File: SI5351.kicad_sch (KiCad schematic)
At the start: 15 parts, among them U8 Si5351A, Y3 25MHz

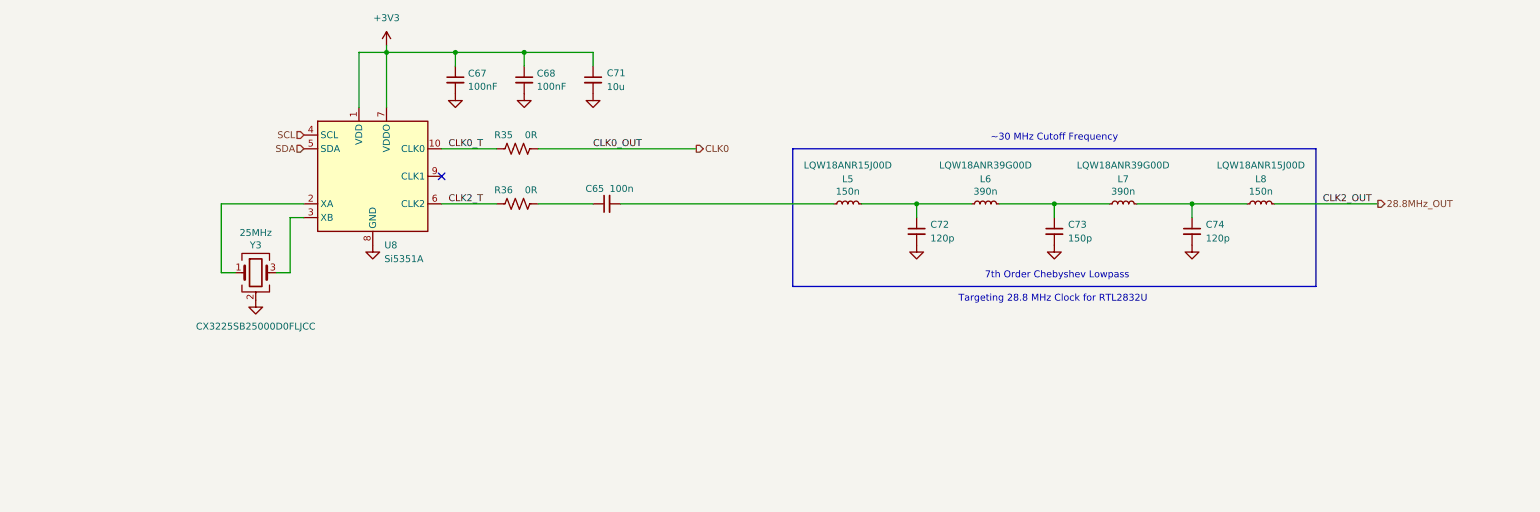
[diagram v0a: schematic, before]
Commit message: Schematic progress
I keep forgetting that I'm just making a panadapter here and not a full blown SDR...oops
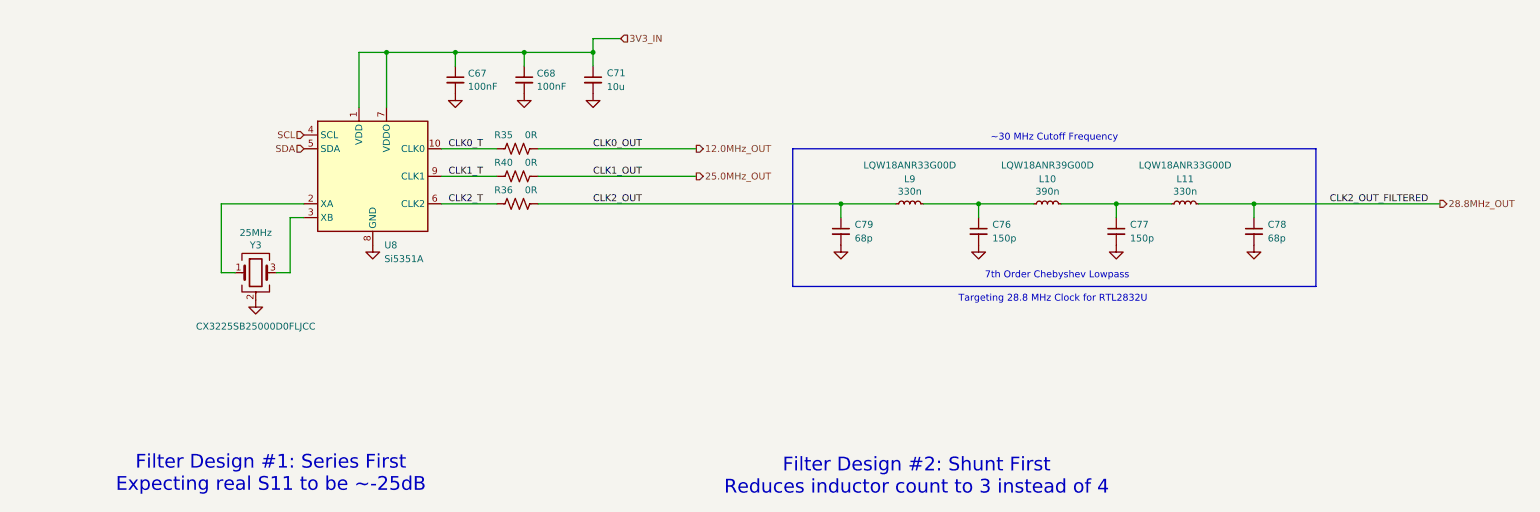
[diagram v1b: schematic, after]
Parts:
- removed C65: 100n, libraries:Worthington_C_0402, symbol Device:C_Small
- removed C72, C74: 120p, Capacitor_SMD:C_0603_1608Metric_Pad1.08x0.95mm_HandSolder, symbol Device:C_Small
- removed C73: 150p, Capacitor_SMD:C_0603_1608Metric_Pad1.08x0.95mm_HandSolder, symbol Device:C_Small
- removed L5, L8: 150n, Inductor_SMD:L_0603_1608Metric, symbol Device:L_Small
- removed L6, L7: 390n, symbol Device:L_Small
- added C76, C77: 150p, Capacitor_SMD:C_0603_1608Metric_Pad1.08x0.95mm_HandSolder, symbol Device:C_Small
- added C78, C79: 68p, Capacitor_SMD:C_0603_1608Metric_Pad1.08x0.95mm_HandSolder, symbol Device:C_Small
- added L10: 390n, libraries:Worthington_L_0603, symbol Device:L_Small
- added L11, L9: 330n, libraries:Worthington_L_0603, symbol Device:L_Small
- added R40: 0R, Resistor_SMD:R_0603_1608Metric_Pad0.98x0.95mm_HandSolder, symbol Device:R_US
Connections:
- net 28.8MHz_OUT: now also C78.1, L11.1
- net GND: now also C76.2, C77.2, C78.2, C79.2
- net CLK1_T: now reaches U8.9 (CLK1)
- net CLK1_T: now also R40.1
- net CLK2_OUT: now reaches R36.2
- net CLK2_OUT: now also C79.1, L9.2
- net +3V3 renamed 3V3_IN
- net CLK0 renamed 12.0MHz_OUT
- new net: C77.1, L10.1, L11.2
- new net: C76.1, L10.2, L9.1
- new net 25.0MHz_OUT: R40.2
- no-connect marks 1 -> 0
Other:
- note added: "Filter Design #1: Series First Expecting real S11 to be ~-25dB"
- note added: "Filter Design #2: Shunt First Reduces inductor count to 3 instead of 4"

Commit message: Schematic progress
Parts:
- removed L10: 390n, libraries:Worthington_L_0603, symbol Device:L_Small
- removed L11, L9: 330n, libraries:Worthington_L_0603, symbol Device:L_Small
- added L18, L20: 330n, libraries:Worthington_L_0603, symbol Device:L_Small
- added L19: 390n, libraries:Worthington_L_0603, symbol Device:L_Small
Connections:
- net 28.8MHz_OUT: now also L20.2
- net CLK2_OUT: now also L18.1
- net at C77.1: now also L19.2, L20.1
- net at C76.1: now also L18.2, L19.1

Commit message: Schematic progress
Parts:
- removed C78: 68p, Capacitor_SMD:C_0603_1608Metric_Pad1.08x0.95mm_HandSolder, symbol Device:C_Small
- added C123, C81: 100n, libraries:Worthington_C_0201, symbol Device:C_Small
- added C92: 68p, libraries:Worthington_C_0201, symbol Device:C_Small
- added R77: 0R, libraries:Worthington_R_0201, symbol Device:R_US
- added R78, R79: 4k7, libraries:Worthington_R_0201, symbol Device:R_Small_US
- C67, C68: value 100nF -> 100n; footprint Capacitor_SMD:C_0603_1608Metric_Pad1.08x0.95mm_HandSolder -> libraries:Worthington_C_0201; DigiKey (none) -> 445-15903-1-ND; Manufacturer Part Number (none) -> C0603X6S1C104K030BC; Voltage (none) -> 16V
- C71: footprint libraries:Worthington_C_0603 -> libraries:Worthington_C_0402; DigiKey (none) -> 4713-GMC04X5R106M10NTCT-ND; Manufacturer Part Number (none) -> GMC04X5R106M10NT; Voltage (none) -> 10V
- C76, C77: footprint Capacitor_SMD:C_0603_1608Metric_Pad1.08x0.95mm_HandSolder -> libraries:Worthington_C_0201; DigiKey (none) -> 4713-GMC02CG151F50NTCT-ND; Manufacturer Part Number (none) -> GMC02CG151F50NT; Voltage (none) -> 50V
- C79: footprint Capacitor_SMD:C_0603_1608Metric_Pad1.08x0.95mm_HandSolder -> libraries:Worthington_C_0201; DigiKey (none) -> 4713-GMC02CG680F50NTCT-ND; Manufacturer Part Number (none) -> GMC02CG680F50NT; Voltage (none) -> 50V
- R35, R36, R40: footprint Resistor_SMD:R_0603_1608Metric_Pad0.98x0.95mm_HandSolder -> libraries:Worthington_R_0201
- U8: value Si5351A -> SI5351B-B-GM1; footprint Package_SO:MSOP-10_3x3mm_P0.5mm -> Package_DFN_QFN:QFN-16-1EP_3x3mm_P0.5mm_EP1.45x1.45mm
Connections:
- net 25.0MHz_OUT: now also R36.2; no longer R40.2
- net 28.8MHz_OUT: now also C92.1
- net 3V3_IN: now also U8.11 (VDDOD), U8.14 (VDDOC), U8.16 (VDD), U8.8 (VDDOB), U8.9 (VDDOA), C123.1, C81.1, R78.2, R79.2; no longer U8.1 (VDD), U8.7 (VDDO)
- net CLK1_T: now also R36.1, U8.7 (CLK1); no longer R40.1, U8.9 (CLK1)
- net CLK2_T: now also R40.1, U8.13 (CLK2); no longer R36.1, U8.6 (CLK2)
- net GND: now also U8.15 (GND), U8.EP (GND), C123.2, C81.2, C92.2; no longer U8.8 (GND)
- net SCL: now also R78.1
- net SDA: now also R79.1
- net at Y3.1: now also U8.1 (XA); no longer U8.2 (XA)
- net at Y3.3: now also U8.2 (XB); no longer U8.3 (XB)
- net CLK2_OUT renamed CLK2
- net CLK2: now also R40.2; no longer R36.2
- new net CLK3_50R_T: R77.1, U8.12 (CLK3)
- new net EXT_CLK_OUT: R77.2
- new net VCXO_IN: U8.3 (VC)
- new net ~{CLK_OUT_EN}: U8.6 (OEB)
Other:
- moved on the sheet: R35, Y3

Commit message: Schematic and PCB progress
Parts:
- renumbered C81 to C66, C123 to C67, C67 to C68, C68 to C69, C71 to C70, C79 to C71, C76 to C72, C77 to C73, C92 to C74, L18 to L5, L19 to L6, L20 to L7, R79 to R50, R78 to R51, R35 to R52, R36 to R53, R40 to R54, R77 to R55, U8 to U10, Y3 to Y1
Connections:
- net GND: now also U10.17 (GND); no longer U10.EP (GND)
- net at Y1.1: now also U10.2 (XB); no longer U10.1 (XA)
- net at Y1.3: now also U10.1 (XA); no longer U10.2 (XB)
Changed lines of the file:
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@@
 		(in_pos_files yes)
 		(dnp no)
-		(property "Reference" "C71"
+		(property "Reference" "C70"
 			(at 171.45 99.0662 0)
 			(show_name no)
@@
 			(project "PiZero_RTL_Panadapter"
 				(path "/9dbbaad8-804a-4efe-a989-bc17c5acbd91/6fef9fcc-556a-4b57-952e-8adf007c871b"
-					(reference "C71")
+					(reference "C70")
 					(unit 1)
 				)
@@
 		(in_pos_files yes)
 		(dnp no)
-		(property "Reference" "L20"
+		(property "Reference" "L7"
 			(at 269.24 118.618 90)
 			(show_name no)
@@
 			(project "PiZero_RTL_Panadapter"
 				(path "/9dbbaad8-804a-4efe-a989-bc17c5acbd91/6fef9fcc-556a-4b57-952e-8adf007c871b"
-					(reference "L20")
+					(reference "L7")
 					(unit 1)
 				)
@@
 		(lib_id "Device:Crystal_GND24")
 		(at 78.74 138.43 0)
-		(unit 1)
-		(body_style 1)
-		(exclude_from_sim no)
-		(in_bom yes)
-		(on_board yes)
-		(in_pos_files yes)
-		(dnp no)
-		(property "Reference" "Y3"
+		(mirror y)
+		(unit 1)
+		(body_style 1)
+		(exclude_from_sim no)
+		(in_bom yes)
+		(on_board yes)
+		(in_pos_files yes)
+		(dnp no)
+		(property "Reference" "Y1"
 			(at 78.74 133.35 0)
 			(show_name no)
@@
 			(project "PiZero_RTL_Panadapter"
 				(path "/9dbbaad8-804a-4efe-a989-bc17c5acbd91/6fef9fcc-556a-4b57-952e-8adf007c871b"
-					(reference "Y3")
+					(reference "Y1")
 					(unit 1)
 				)
@@
 		(in_pos_files yes)
 		(dnp no)
-		(property "Reference" "L19"
+		(property "Reference" "L6"
 			(at 243.84 118.618 90)
 			(show_name no)
@@
 			(project "PiZero_RTL_Panadapter"
 				(path "/9dbbaad8-804a-4efe-a989-bc17c5acbd91/6fef9fcc-556a-4b57-952e-8adf007c871b"
-					(reference "L19")
+					(reference "L6")
 					(unit 1)
 				)
@@
 		(in_pos_files yes)
 		(dnp no)
-		(property "Reference" "C81"
+		(property "Reference" "C66"
 			(at 130.81 99.0662 0)
 			(show_name no)
@@
 			(project "PiZero_RTL_Panadapter"
 				(path "/9dbbaad8-804a-4efe-a989-bc17c5acbd91/6fef9fcc-556a-4b57-952e-8adf007c871b"
-					(reference "C81")
+					(reference "C66")
 					(unit 1)
 				)
@@
 		(in_pos_files yes)
 		(dnp no)
-		(property "Reference" "C68"
+		(property "Reference" "C69"
 			(at 161.29 99.0662 0)
 			(show_name no)
@@
 			(project "PiZero_RTL_Panadapter"
 				(path "/9dbbaad8-804a-4efe-a989-bc17c5acbd91/6fef9fcc-556a-4b57-952e-8adf007c871b"
-					(reference "C68")
+					(reference "C69")
 					(unit 1)
 				)
@@
 		(in_pos_files yes)
 		(dnp no)
-		(property "Reference" "U8"
+		(property "Reference" "U10"
 			(at 108.458 119.888 0)
 			(show_name no)
@@
 		(pin "13"
 		)
-		(pin "EP"
+		(pin "17"
 		)
 		(pin "16"
@@
 			(project "PiZero_RTL_Panadapter"
 				(path "/9dbbaad8-804a-4efe-a989-bc17c5acbd91/6fef9fcc-556a-4b57-952e-8adf007c871b"
-					(reference "U8")
+					(reference "U10")
 					(unit 1)
 				)
@@
 		(in_pos_files yes)
 		(dnp no)
-		(property "Reference" "C79"
+		(property "Reference" "C71"
 			(at 208.28 127.0062 0)
 			(show_name no)
@@
 			(project "PiZero_RTL_Panadapter"
 				(path "/9dbbaad8-804a-4efe-a989-bc17c5acbd91/6fef9fcc-556a-4b57-952e-8adf007c871b"
-					(reference "C79")
+					(reference "C71")
 					(unit 1)
 				)
@@
 		(dnp no)
 		(fields_autoplaced yes)
-		(property "Reference" "#PWR0132"
+		(property "Reference" "#PWR0102"
 			(at 138.43 109.22 0)
 			(hide yes)
@@
 			(project "PiZero_RTL_Panadapter"
 				(path "/9dbbaad8-804a-4efe-a989-bc17c5acbd91/6fef9fcc-556a-4b57-952e-8adf007c871b"
-					(reference "#PWR0132")
+					(reference "#PWR0102")
 					(unit 1)
 				)
@@
 		(in_pos_files yes)
 		(dnp no)
-		(property "Reference" "R79"
+		(property "Reference" "R50"
 			(at 69.342 105.156 0)
 			(show_name no)
@@
 			(project "PiZero_RTL_Panadapter"
 				(path "/9dbbaad8-804a-4efe-a989-bc17c5acbd91/6fef9fcc-556a-4b57-952e-8adf007c871b"
-					(reference "R79")
+					(reference "R50")
 					(unit 1)
 				)
@@
 		(in_pos_files yes)
 		(dnp no)
-		(property "Reference" "C92"
+		(property "Reference" "C74"
 			(at 284.48 127.0062 0)
 			(show_name no)
@@
 			(project "PiZero_RTL_Panadapter"
 				(path "/9dbbaad8-804a-4efe-a989-bc17c5acbd91/6fef9fcc-556a-4b57-952e-8adf007c871b"
-					(reference "C92")
+					(reference "C74")
 					(unit 1)
 				)
@@
 		(in_pos_files yes)
 		(dnp no)
-		(property "Reference" "R77"
+		(property "Reference" "R55"
 			(at 149.86 125.73 90)
 			(show_name no)
@@
 			(project "PiZero_RTL_Panadapter"
 				(path "/9dbbaad8-804a-4efe-a989-bc17c5acbd91/6fef9fcc-556a-4b57-952e-8adf007c871b"
-					(reference "R77")
+					(reference "R55")
 					(unit 1)
 				)
@@
 		(in_pos_files yes)
 		(dnp no)
-		(property "Reference" "R78"
+		(property "Reference" "R51"
 			(at 79.502 105.156 0)
 			(show_name no)
@@
 			(project "PiZero_RTL_Panadapter"
 				(path "/9dbbaad8-804a-4efe-a989-bc17c5acbd91/6fef9fcc-556a-4b57-952e-8adf007c871b"
-					(reference "R78")
+					(reference "R51")
 					(unit 1)
 				)
@@
 		(in_pos_files yes)
 		(dnp no)
-		(property "Reference" "R35"
+		(property "Reference" "R52"
 			(at 149.86 110.49 90)
 			(show_name no)
@@
 			(project "PiZero_RTL_Panadapter"
 				(path "/9dbbaad8-804a-4efe-a989-bc17c5acbd91/6fef9fcc-556a-4b57-952e-8adf007c871b"
-					(reference "R35")
+					(reference "R52")
 					(unit 1)
 				)
@@
 		(in_pos_files yes)
 		(dnp no)
-		(property "Reference" "R40"
+		(property "Reference" "R54"
 			(at 149.86 120.65 90)
 			(show_name no)
@@
 			(project "PiZero_RTL_Panadapter"
 				(path "/9dbbaad8-804a-4efe-a989-bc17c5acbd91/6fef9fcc-556a-4b57-952e-8adf007c871b"
-					(reference "R40")
+					(reference "R54")
 					(unit 1)
 				)
@@
 		(dnp no)
 		(fields_autoplaced yes)
-		(property "Reference" "#PWR0131"
+		(property "Reference" "#PWR0101"
 			(at 128.27 109.22 0)
 			(hide yes)
@@
 			(project "PiZero_RTL_Panadapter"
 				(path "/9dbbaad8-804a-4efe-a989-bc17c5acbd91/6fef9fcc-556a-4b57-952e-8adf007c871b"
-					(reference "#PWR0131")
+					(reference "#PWR0101")
 					(unit 1)
 				)
@@
 		(in_pos_files yes)
 		(dnp no)
-		(property "Reference" "L18"
+		(property "Reference" "L5"
 			(at 218.44 118.618 90)
 			(show_name no)
@@
 			(project "PiZero_RTL_Panadapter"
 				(path "/9dbbaad8-804a-4efe-a989-bc17c5acbd91/6fef9fcc-556a-4b57-952e-8adf007c871b"
-					(reference "L18")
+					(reference "L5")
 					(unit 1)
 				)
@@
 		(dnp no)
 		(fields_autoplaced yes)
-		(property "Reference" "#PWR0114"
+		(property "Reference" "#PWR0106"
 			(at 205.74 137.16 0)
 			(hide yes)
@@
 			(project "PiZero_RTL_Panadapter"
 				(path "/9dbbaad8-804a-4efe-a989-bc17c5acbd91/6fef9fcc-556a-4b57-952e-8adf007c871b"
-					(reference "#PWR0114")
+					(reference "#PWR0106")
 					(unit 1)
 				)
@@
 		(dnp no)
 		(fields_autoplaced yes)
-		(property "Reference" "#PWR0113"
+		(property "Reference" "#PWR0109"
 			(at 281.94 137.16 0)
 			(hide yes)
@@
 			(project "PiZero_RTL_Panadapter"
 				(path "/9dbbaad8-804a-4efe-a989-bc17c5acbd91/6fef9fcc-556a-4b57-952e-8adf007c871b"
-					(reference "#PWR0113")
+					(reference "#PWR0109")
 					(unit 1)
 				)
@@
 		(in_pos_files yes)
 		(dnp no)
-		(property "Reference" "C123"
+		(property "Reference" "C67"
 			(at 140.97 99.0662 0)
 			(show_name no)
@@
 			(project "PiZero_RTL_Panadapter"
 				(path "/9dbbaad8-804a-4efe-a989-bc17c5acbd91/6fef9fcc-556a-4b57-952e-8adf007c871b"
-					(reference "C123")
+					(reference "C67")
 					(unit 1)
 				)
@@
 		(in_pos_files yes)
 		(dnp no)
-		(property "Reference" "C77"
+		(property "Reference" "C73"
 			(at 259.08 127.0062 0)
 			(show_name no)
@@
 			(project "PiZero_RTL_Panadapter"
 				(path "/9dbbaad8-804a-4efe-a989-bc17c5acbd91/6fef9fcc-556a-4b57-952e-8adf007c871b"
-					(reference "C77")
+					(reference "C73")
 					(unit 1)
 				)
@@
 		(dnp no)
 		(fields_autoplaced yes)
-		(property "Reference" "#PWR0112"
+		(property "Reference" "#PWR0108"
 			(at 256.54 137.16 0)
 			(hide yes)
@@
 			(project "PiZero_RTL_Panadapter"
 				(path "/9dbbaad8-804a-4efe-a989-bc17c5acbd91/6fef9fcc-556a-4b57-952e-8adf007c871b"
-					(reference "#PWR0112")
+					(reference "#PWR0108")
 					(unit 1)
 				)
@@
 		(dnp no)
 		(fields_autoplaced yes)
-		(property "Reference" "#PWR0101"
+		(property "Reference" "#PWR099"
 			(at 78.74 149.86 0)
 			(hide yes)
@@
 			(project "PiZero_RTL_Panadapter"
 				(path "/9dbbaad8-804a-4efe-a989-bc17c5acbd91/6fef9fcc-556a-4b57-952e-8adf007c871b"
-					(reference "#PWR0101")
+					(reference "#PWR099")
 					(unit 1)
 				)
@@
 		(in_pos_files yes)
 		(dnp no)
-		(property "Reference" "C67"
+		(property "Reference" "C68"
 			(at 151.13 99.0662 0)
 			(show_name no)
@@
 			(project "PiZero_RTL_Panadapter"
 				(path "/9dbbaad8-804a-4efe-a989-bc17c5acbd91/6fef9fcc-556a-4b57-952e-8adf007c871b"
-					(reference "C67")
+					(reference "C68")
 					(unit 1)
 				)
@@
 		(in_pos_files yes)
 		(dnp no)
-		(property "Reference" "C76"
+		(property "Reference" "C72"
 			(at 233.68 127.0062 0)
 			(show_name no)
@@
 			(project "PiZero_RTL_Panadapter"
 				(path "/9dbbaad8-804a-4efe-a989-bc17c5acbd91/6fef9fcc-556a-4b57-952e-8adf007c871b"
-					(reference "C76")
+					(reference "C72")
 					(unit 1)
 				)
@@
 		(dnp no)
 		(fields_autoplaced yes)
-		(property "Reference" "#PWR0111"
+		(property "Reference" "#PWR0107"
 			(at 231.14 137.16 0)
 			(hide yes)
@@
 			(project "PiZero_RTL_Panadapter"
 				(path "/9dbbaad8-804a-4efe-a989-bc17c5acbd91/6fef9fcc-556a-4b57-952e-8adf007c871b"
-					(reference "#PWR0111")
+					(reference "#PWR0107")
 					(unit 1)
 				)
@@
 		(in_pos_files yes)
 		(dnp no)
-		(property "Reference" "R36"
+		(property "Reference" "R53"
 			(at 149.86 115.57 90)
 			(show_name no)
@@
 			(project "PiZero_RTL_Panadapter"
 				(path "/9dbbaad8-804a-4efe-a989-bc17c5acbd91/6fef9fcc-556a-4b57-952e-8adf007c871b"
-					(reference "R36")
-					(unit 1)
-				)
+					(reference "R53")
+					(unit 1)
+				)

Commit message: PCB Layout Progress
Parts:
- added C90: 100n, libraries:Worthington_C_0201, symbol Device:C_Small
- C71, C74: value 68p -> 68p, ±1%
- C72, C73: value 150p -> 150p, ±1%
- L5, L7: value 330n -> 330n, ±2%; footprint libraries:Worthington_L_0603 -> libraries:Worthington_L_0603_RF
- L6: value 390n -> 390n, ±2%; footprint libraries:Worthington_L_0603 -> libraries:Worthington_L_0603_RF
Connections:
- net 12.0MHz_OUT: now also R54.2; no longer R52.2
- net 3V3_IN: now also C90.1
- net GND: now also C90.2
- net CLK2 renamed CLK0
- net CLK0: now also R52.2; no longer R54.2
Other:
- moved on the sheet: C66, C67, C68, C69, C70, C71, C72, C73, C74, L5, L6, L7

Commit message: PCB and schematic progress
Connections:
- net 25.0MHz_OUT: now also R52.2; no longer R53.2
- net CLK0 renamed CLK1
- net CLK1: now also R53.2; no longer R52.2
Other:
- moved on the sheet: C71, C72, C73, C74, L5, L6, L7
